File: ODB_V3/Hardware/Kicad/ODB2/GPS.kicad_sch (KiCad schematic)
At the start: 22 parts, among them IC2 ZED-F9P-15B, J1 RF2-04A-T-00-50-G, J4 RF2-04A-T-00-50-G, U5 L76L-M33

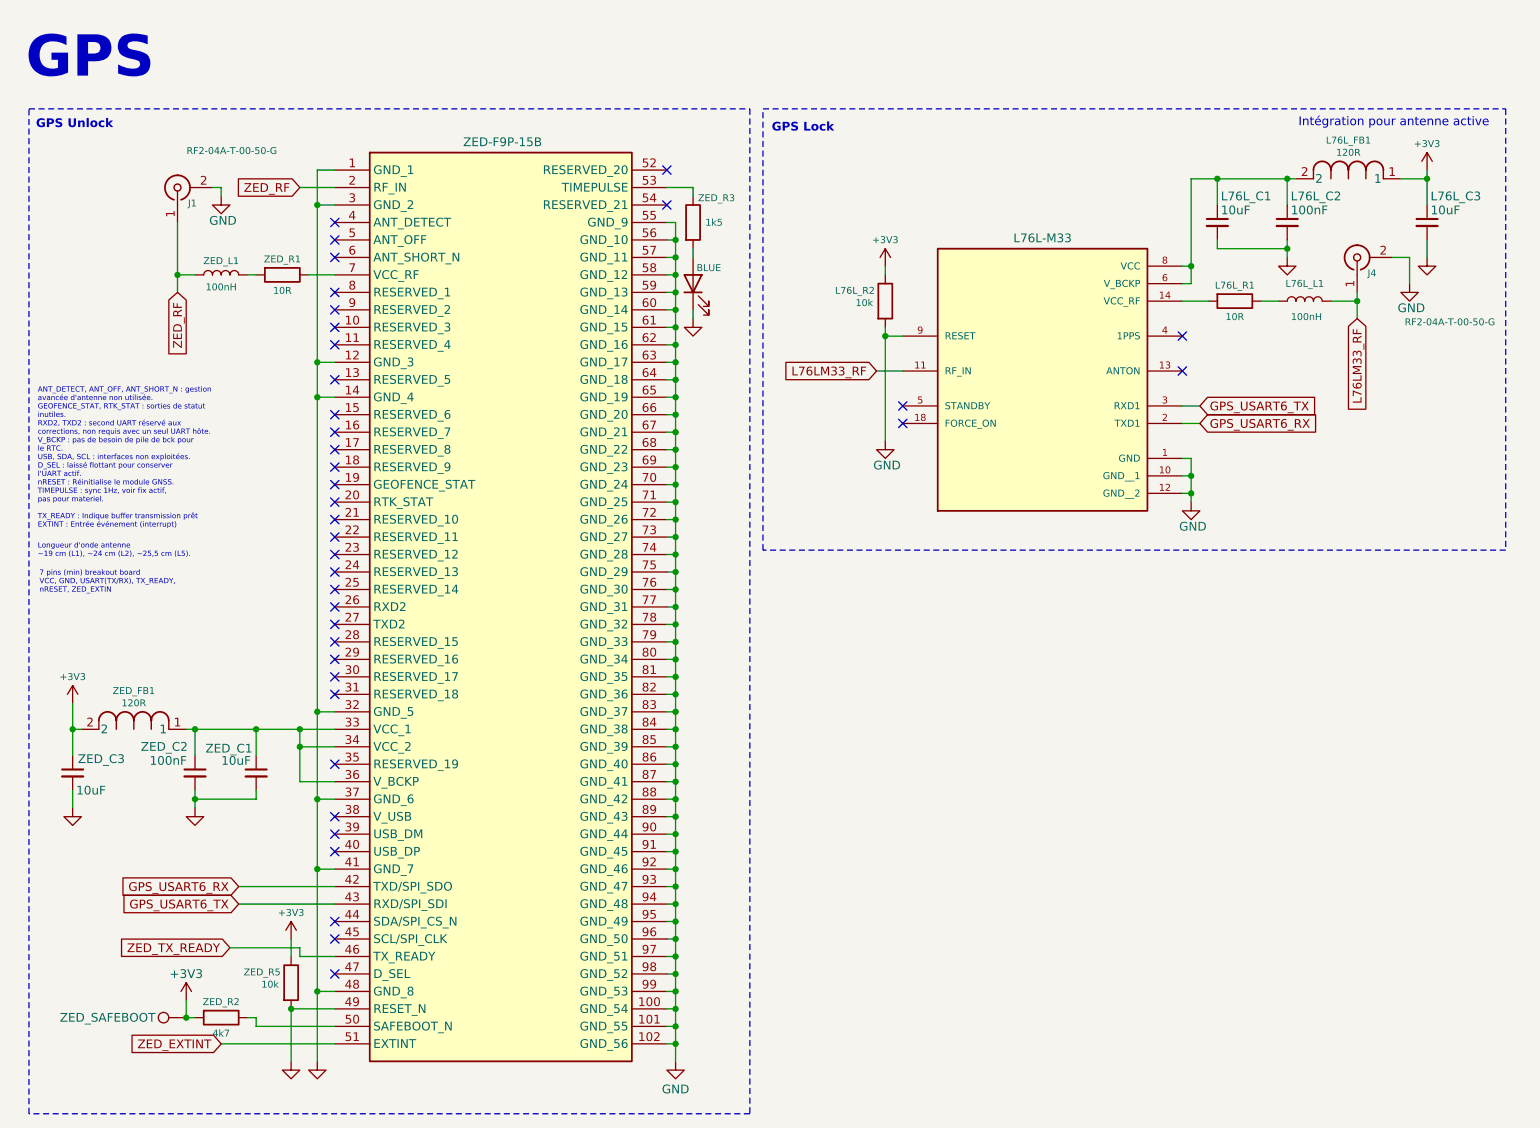
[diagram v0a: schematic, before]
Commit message: fix: decoupling capacitance gps
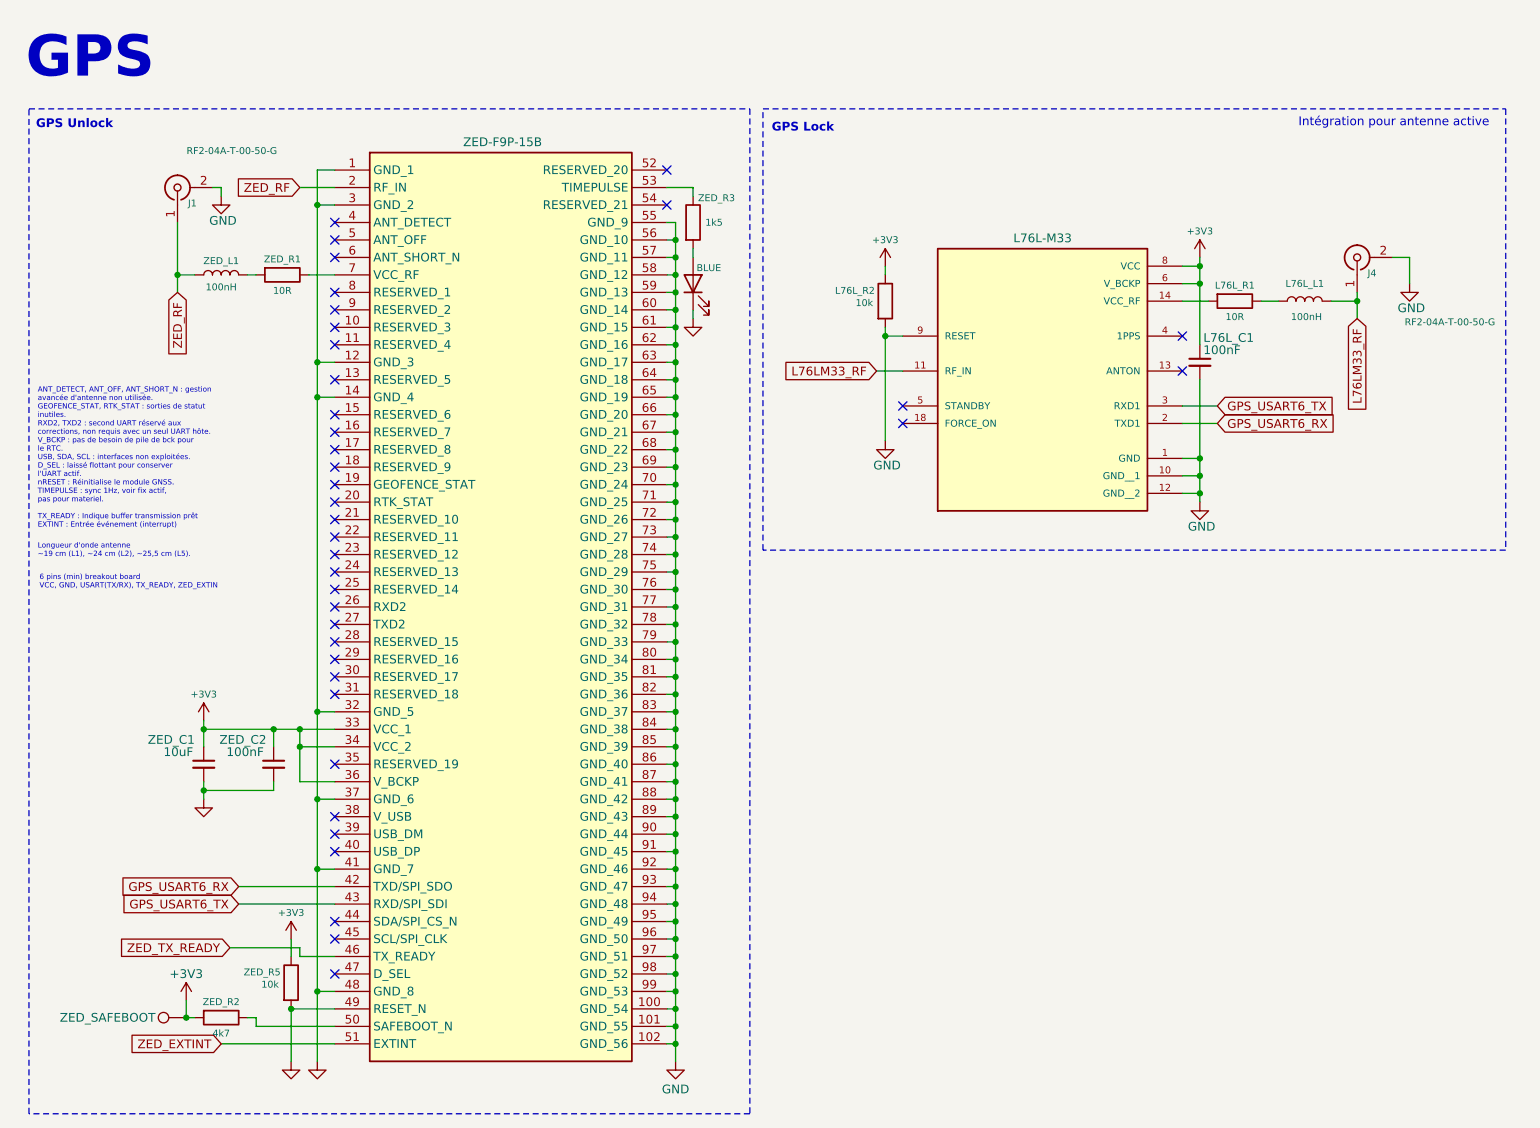
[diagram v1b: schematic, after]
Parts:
- removed L76L_C2: 100nF, Capacitor_SMD:C_0603_1608Metric, symbol Device:C_Small
- removed L76L_C3, ZED_C3: 10uF, Capacitor_SMD:C_0603_1608Metric, symbol Device:C_Small
- removed L76L_FB1, ZED_FB1: 120R, IND_25_0805_FRT, symbol ODB2:2508051217Y6
- L76L_C1: value 10uF -> 100nF
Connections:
- net +3V3: now also IC2.33 (VCC_1), IC2.34 (VCC_2), IC2.36 (V_BCKP), L76L_C1.1, U5.6 (V_BCKP), U5.8 (VCC), ZED_C1.1, ZED_C2.1
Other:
- note added: "6 pins (min) breakout board VCC, GND, USART(TX/RX), TX_READY, ZED_EXTIN"
- note removed: "7 pins (min) breakout board VCC, GND, USART(TX/RX), TX_READY, nRESET, ZED_EXTIN"

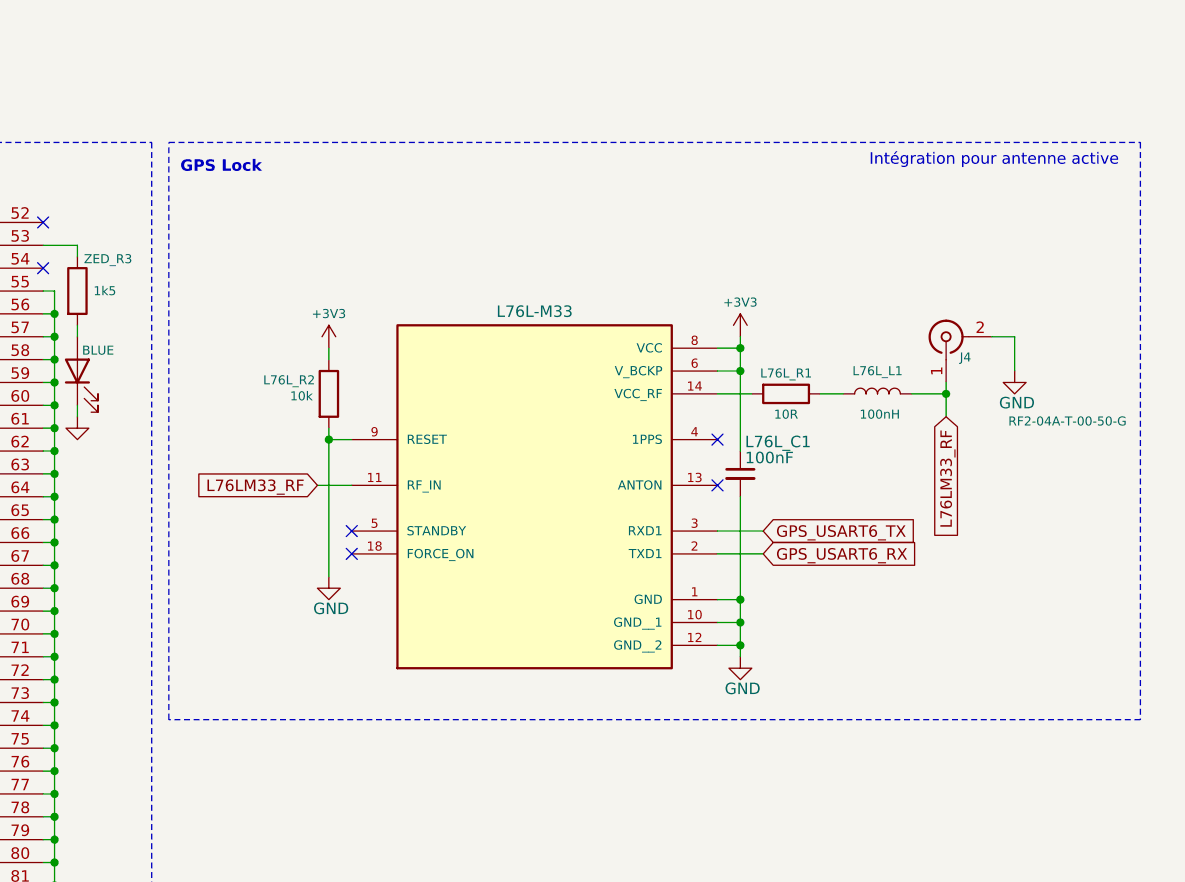
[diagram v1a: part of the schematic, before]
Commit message: feat: add mem2067
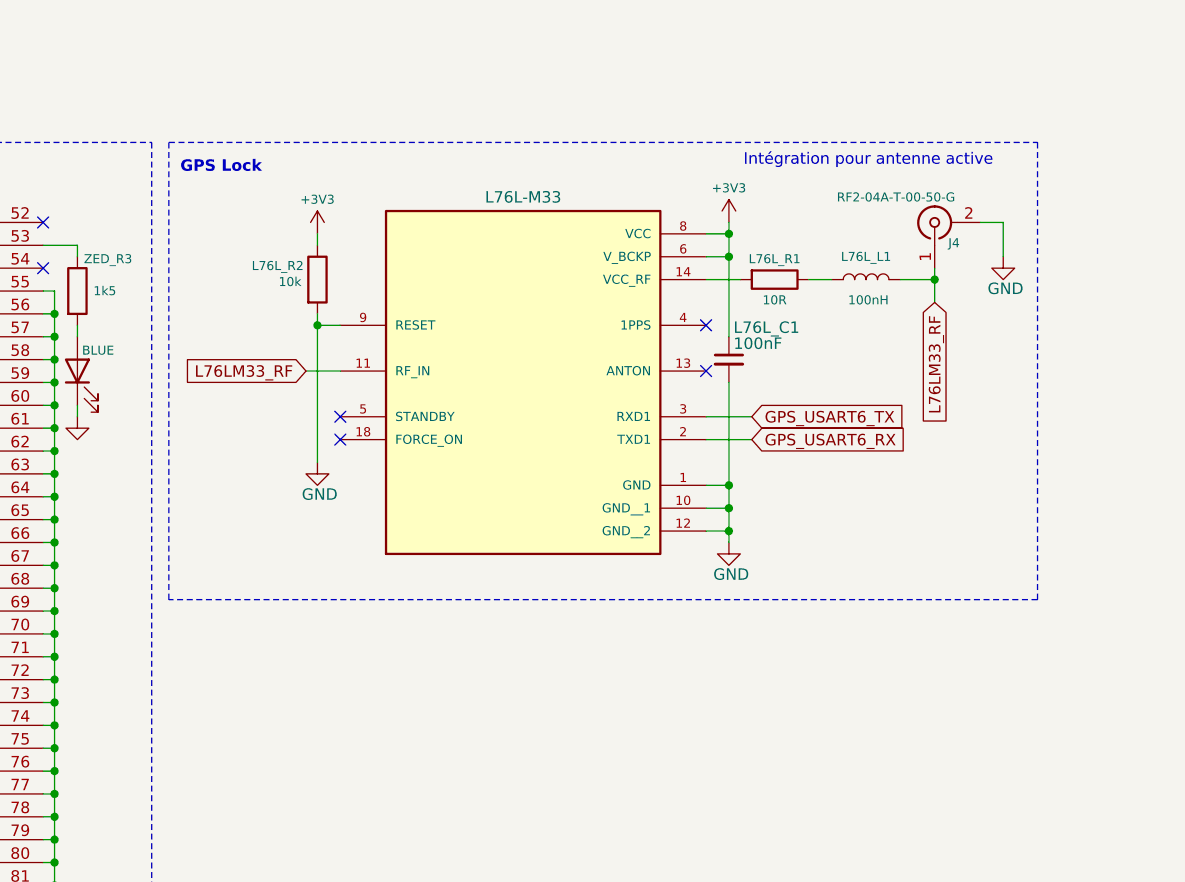
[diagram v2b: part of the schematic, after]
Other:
- moved on the sheet: J4, L76L_C1, L76L_L1, L76L_R1, L76L_R2

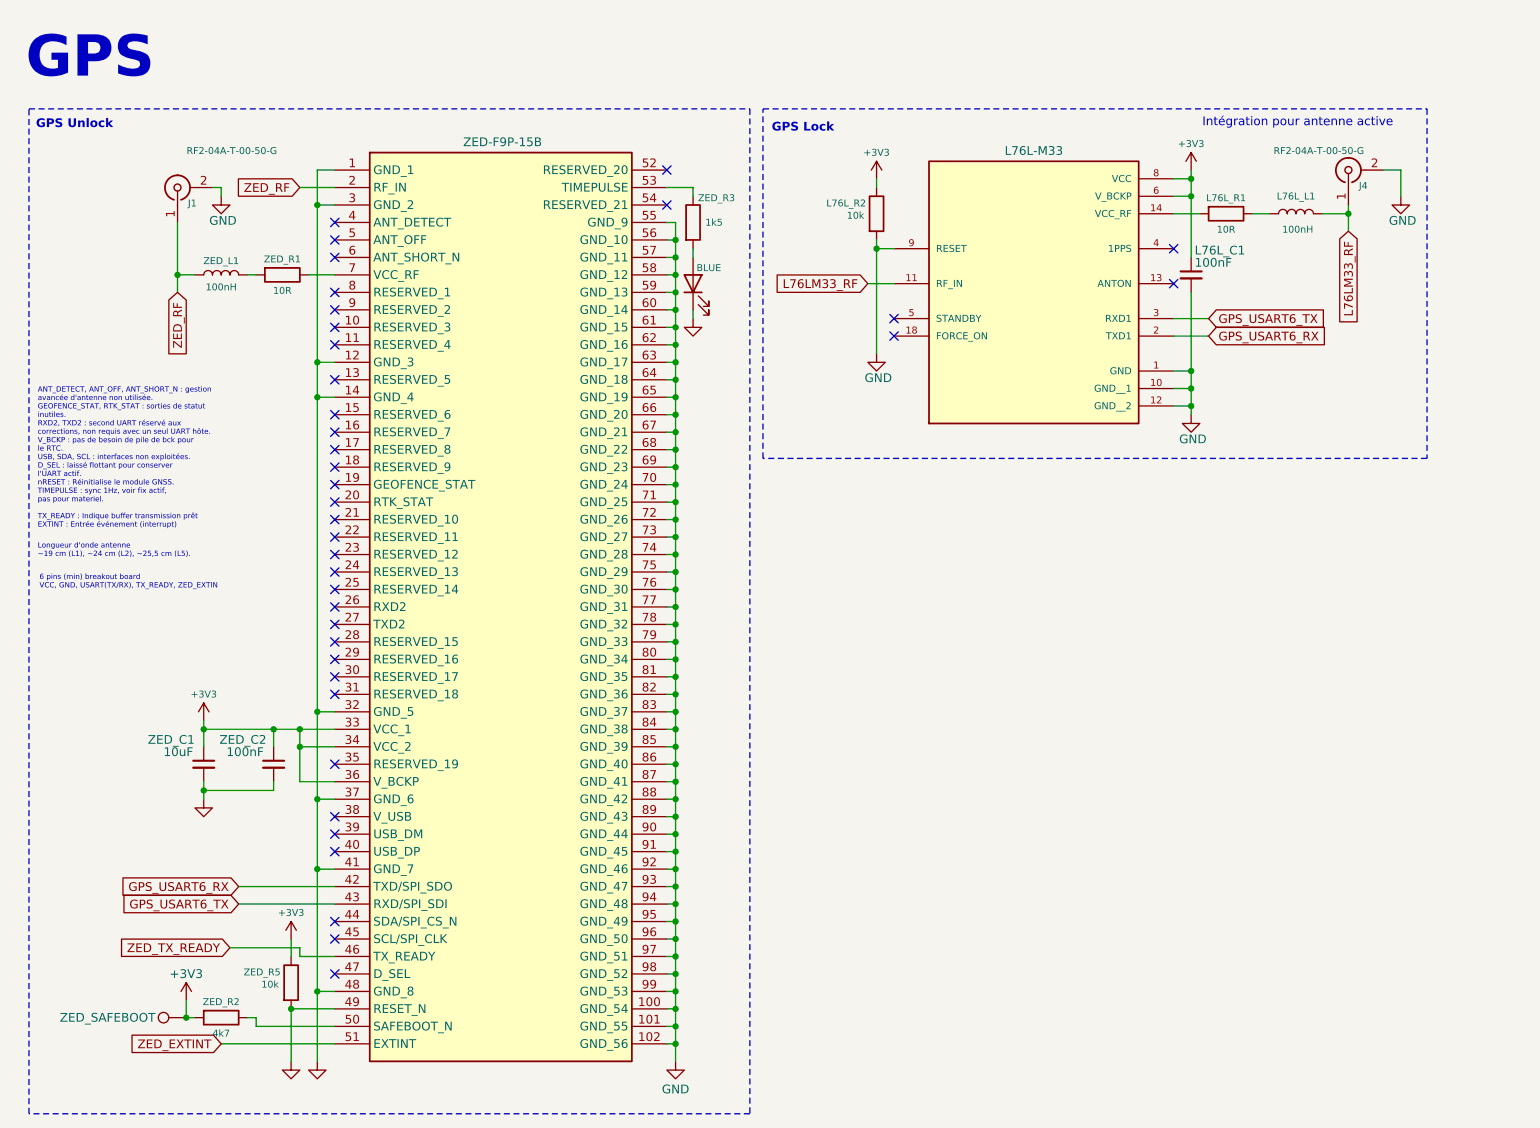
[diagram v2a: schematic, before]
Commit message: fix: gps page remove
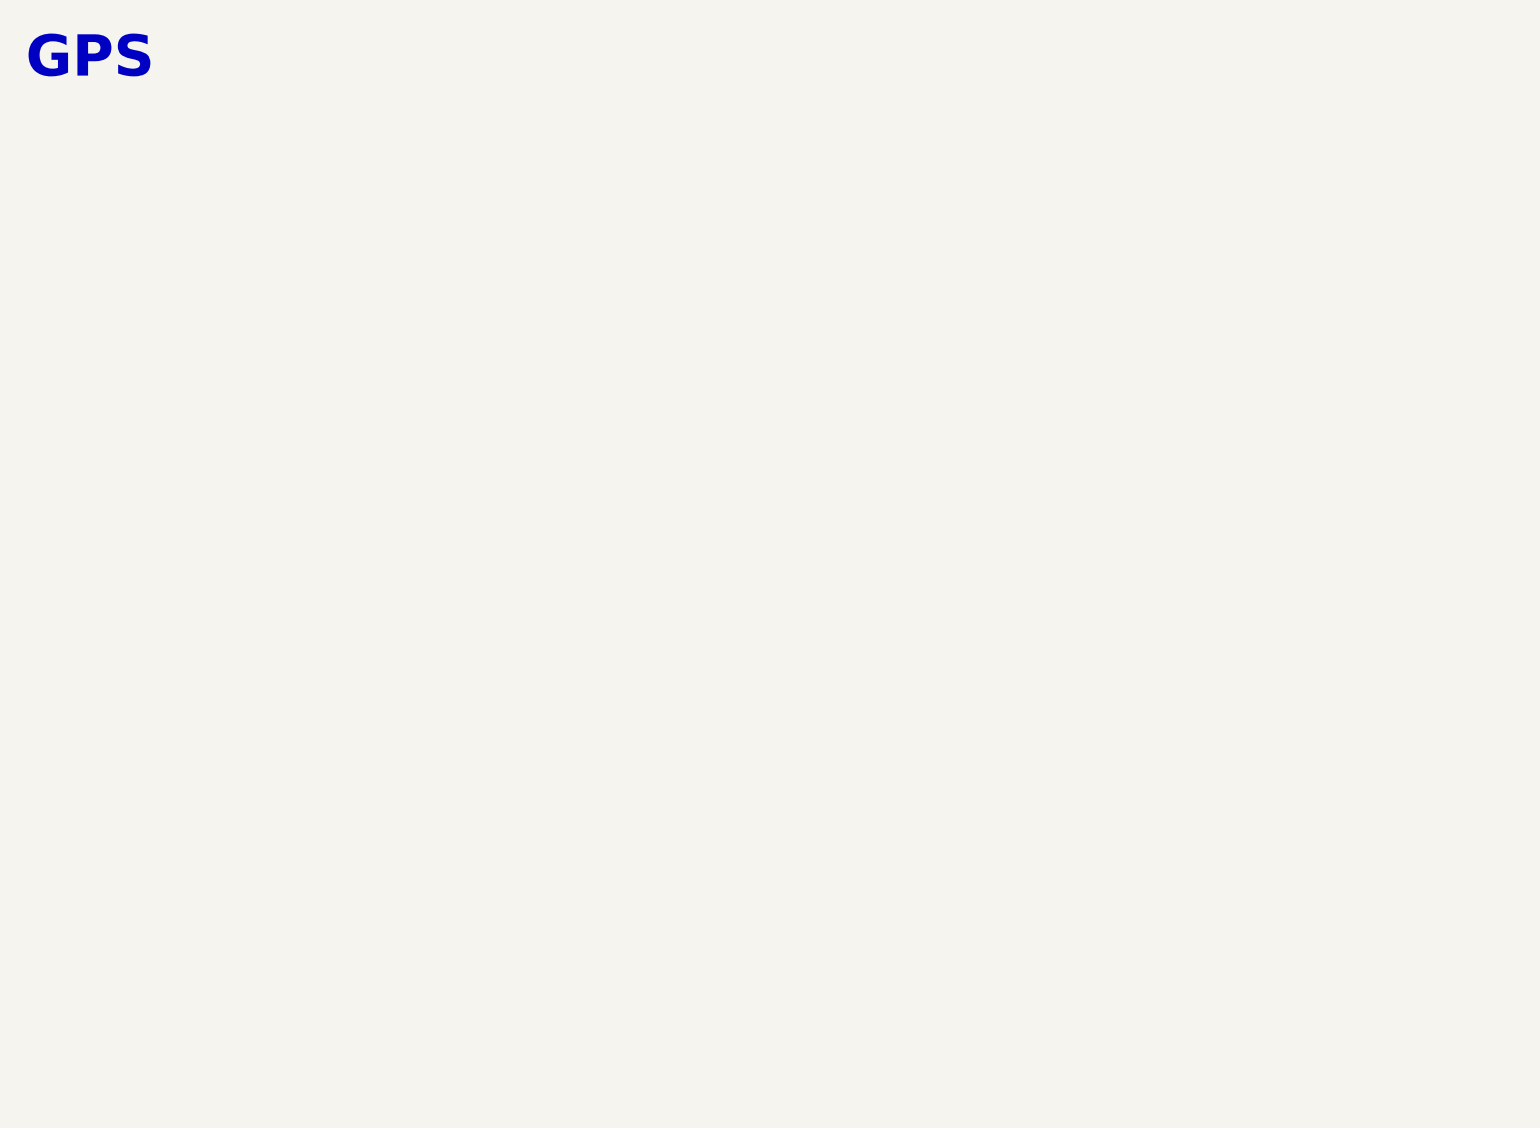
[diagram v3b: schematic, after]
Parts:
- removed BT_LED2: BLUE, LED_SMD:LED_0603_1608Metric, symbol Device:LED
- removed IC2: ZED-F9P-15B, ZEDF9P15B, symbol ODB2:ZED-F9P-15B
- removed J1, J4: RF2-04A-T-00-50-G, Connector_Coaxial:SMA_Wurth_60312002114503_Vertical, symbol Connector:Conn_Coaxial
- removed L76L_C1, ZED_C2: 100nF, Capacitor_SMD:C_0603_1608Metric, symbol Device:C_Small
- removed L76L_L1, ZED_L1: 100nH, Inductor_SMD:L_0603_1608Metric, symbol Device:L
- removed L76L_R1, ZED_R1: 10R, Resistor_SMD:R_0603_1608Metric, symbol Device:R
- removed L76L_R2, ZED_R5: 10k, Resistor_SMD:R_0603_1608Metric, symbol Device:R
- removed U5: L76L-M33, L76L-M33:XCVR_L76L-M33, symbol ODB2:L76L-M33
- removed ZED_C1: 10uF, Capacitor_SMD:C_0603_1608Metric, symbol Device:C_Small
- removed ZED_R2: 4k7, Resistor_SMD:R_0603_1608Metric, symbol Device:R
- removed ZED_R3: 1k5, Resistor_SMD:R_0603_1608Metric, symbol Device:R
- removed ZED_SAFEBOOT: TestPoint, TestPoint:TestPoint_Pad_D1.0mm, symbol Connector:TestPoint
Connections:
- no-connect marks 38 -> 0
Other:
- note removed: "6 pins (min) breakout board VCC, GND, USART(TX/RX), TX_READY, ZED_EXTIN"
- note removed: "ANT_DETECT, ANT_OFF, ANT_SHORT_N : gestion avancée d'antenne non utilisée. GEOFENCE_STAT, RTK_STAT : sorties de statut inutiles. RXD2, TXD2 : second UART réservé aux corrections, non requis avec un seul UART hôte. V_BCKP : pas de besoin de pile de bck pour le RTC. USB, SDA, SCL : interfaces non exploitées. D_SEL : laissé flottant pour conserver l'UART actif. nRESET : Réinitialise le module GNSS. 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"
- note removed: "GPS Lock"
- note removed: "GPS Unlock"
- note removed: "Intégration pour antenne active"
- note removed: "Longueur d'onde antenne ~19 cm (L1), ~24 cm (L2), ~25,5 cm (L5)."
